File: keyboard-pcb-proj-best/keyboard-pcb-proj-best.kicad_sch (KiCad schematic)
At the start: 0 parts

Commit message: Built Schematic
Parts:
- added C1: 1uF, Capacitor_SMD:C_0805_2012Metric_Pad1.18x1.45mm_HandSolder, symbol Device:C_Small
- added C2, C3, C4: 0.1uF, Capacitor_SMD:C_0805_2012Metric_Pad1.18x1.45mm_HandSolder, symbol Device:C_Small
- added C5: 10uf, Capacitor_SMD:C_0805_2012Metric_Pad1.18x1.45mm_HandSolder, symbol Device:C_Small
- added C6, C7: 22pF, Capacitor_SMD:C_0805_2012Metric_Pad1.18x1.45mm_HandSolder, symbol Device:C_Small
- added D1, D2, D3, D4: SOD-123, Diode_SMD:D_SOD-123, symbol Device:D_Small
- added F1: 500mA, Fuse:Fuse_1206_3216Metric, symbol Device:Polyfuse
- added MX1, MX2, MX3, MX4: MX-NoLED, MX_Alps_Hybrid:MX-10U-NoLED, symbol MX_Alps_Hybrid:MX-NoLED
- added R1, R4: 10k, Resistor_SMD:R_0805_2012Metric, symbol Device:R_Small
- added R2, R3: 22, Resistor_SMD:R_0805_2012Metric, symbol Device:R_Small
- added SW1: SW_PUSH, random-keyboard-parts:SKQG-1155865, symbol keyboard_parts:SW_PUSH
- added U1: ATmega32U4-A, Package_QFP:TQFP-44_10x10mm_P0.8mm, symbol MCU_Microchip_ATmega:ATmega32U4-A
- added USB1: Molex-0548190589, random-keyboard-parts:Molex-0548190589, symbol random-keyboard-parts:Molex-0548190589
- added Y1: 16Mhz, Crystal:Crystal_SMD_3225-4Pin_3.2x2.5mm, symbol Device:Crystal_GND24_Small
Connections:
- new net: R4.2, SW1.2, U1.13 (~{RESET})
- new net: C7.2, U1.16 (XTAL2), Y1.3
- new net: C6.2, U1.17 (XTAL1), Y1.1
- new net: R3.1, U1.3 (D-)
- new net: R1.2, U1.33 (~{HWB}/PE2)
- new net: R2.1, U1.4 (D+)
- new net: C1.1, U1.6 (UCAP)
- new net: D2.2 (A), MX2.2 (ROW)
- new net: D3.2 (A), MX3.2 (ROW)
- new net: D4.2 (A), MX4.2 (ROW)
- new net: D1.2 (A), MX1.2 (ROW)
- new net +5V: C2.1, C3.1, C4.1, C5.1, F1.1, R4.1, U1.14 (VCC), U1.2 (UVCC), U1.24 (AVCC), U1.34 (VCC), U1.44 (AVCC), U1.7 (VBUS)
- new net COL0: MX1.1 (COL), MX3.1 (COL)
- new net COL1: MX2.1 (COL), MX4.1 (COL)
- new net D+: R2.2, USB1.3 (D+)
- new net D-: R3.2, USB1.4 (D-)
- new net GND: C1.2, C2.2, C3.2, C4.2, C5.2, C6.1, C7.1, R1.1, SW1.1, U1.15 (GND), U1.23 (GND), U1.35 (GND), U1.43 (GND), U1.5 (UGND), USB1.1 (GND), Y1.2, Y1.4
- new net ROW0: D1.1 (K), D2.1 (K)
- new net ROW1: D3.1 (K), D4.1 (K)
- new net VCC: F1.2, USB1.5 (VBUS)

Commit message: Created PCB
Still need to finish routing
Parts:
- MX1, MX2, MX3, MX4: footprint MX_Alps_Hybrid:MX-10U-NoLED -> MX_Alps_Hybrid:MX-1U-NoLED
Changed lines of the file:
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@@
 			)
 		)
-		(property "Footprint" "MX_Alps_Hybrid:MX-10U-NoLED"
+		(property "Footprint" "MX_Alps_Hybrid:MX-1U-NoLED"
 			(at 146.685 90.805 0)
 			(effects
@@
 			)
 		)
-		(property "Footprint" "MX_Alps_Hybrid:MX-10U-NoLED"
+		(property "Footprint" "MX_Alps_Hybrid:MX-1U-NoLED"
 			(at 132.715 107.315 0)
 			(effects
@@
 			)
 		)
-		(property "Footprint" "MX_Alps_Hybrid:MX-10U-NoLED"
+		(property "Footprint" "MX_Alps_Hybrid:MX-1U-NoLED"
 			(at 132.715 90.805 0)
 			(effects
@@
 			)
 		)
-		(property "Footprint" "MX_Alps_Hybrid:MX-10U-NoLED"
+		(property "Footprint" "MX_Alps_Hybrid:MX-1U-NoLED"
 			(at 146.685 107.315 0)
 			(effects

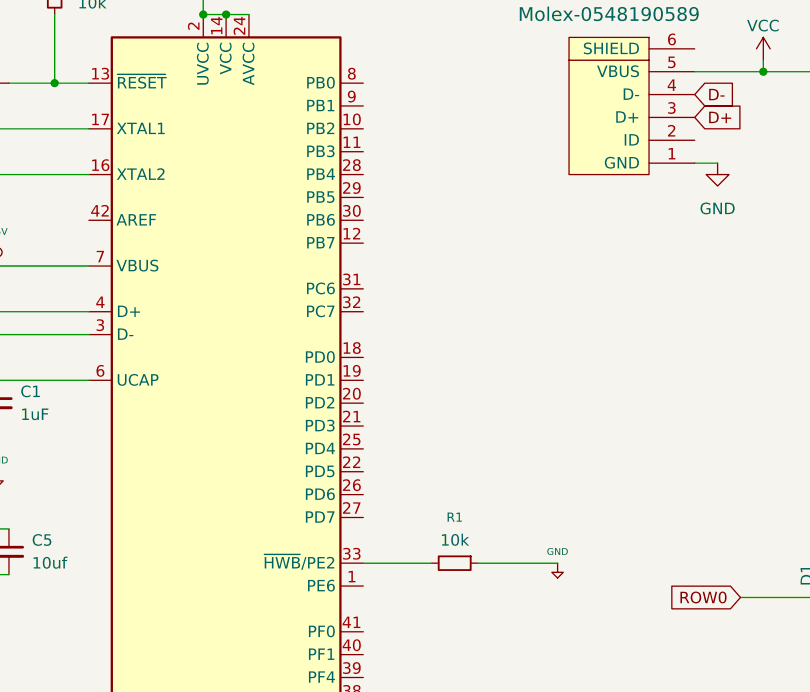
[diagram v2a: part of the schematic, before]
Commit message: Finalized Routing and Matrix Pin Out
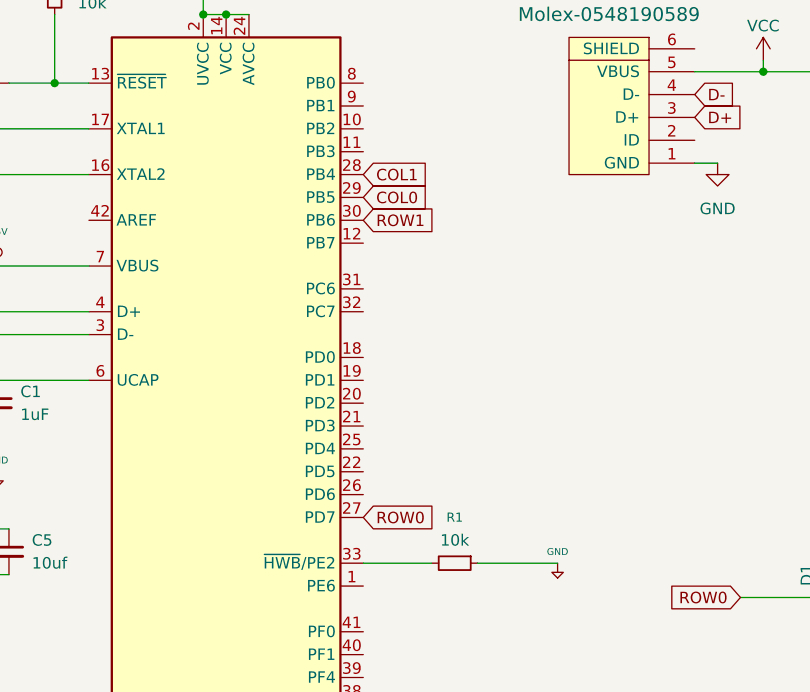
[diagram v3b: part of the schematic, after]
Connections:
- net COL0: now also U1.29 (PB5)
- net COL1: now also U1.28 (PB4)
- net ROW0: now also U1.27 (PD7)
- net ROW1: now also U1.30 (PB6)
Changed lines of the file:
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@@
+		)
+	)
+	(global_label "COL1"
+		(shape input)
+		(at 88.9 53.34 0)
+		(fields_autoplaced yes)
+		(effects
+			(font
+				(size 1.27 1.27)
+			)
+			(justify left)
+		)
+		(property "Intersheetrefs" "${INTERSHEET_REFS}"
+			(at 96.7233 53.34 0)
+			(effects
+				(font
+					(size 1.27 1.27)
+				)
+				(justify left)
+				(hide yes)
+			)
 		)
 	)
@@
 		)
 	)
+	(global_label "ROW1"
+		(shape input)
+		(at 88.9 58.42 0)
+		(fields_autoplaced yes)
+		(effects
+			(font
+				(size 1.27 1.27)
+			)
+			(justify left)
+		)
+		(property "Intersheetrefs" "${INTERSHEET_REFS}"
+			(at 97.1466 58.42 0)
+			(effects
+				(font
+					(size 1.27 1.27)
+				)
+				(justify left)
+				(hide yes)
+			)
+		)
+	)
 	(global_label "D-"
 		(shape input)
@@
 		)
 	)
+	(global_label "ROW0"
+		(shape input)
+		(at 88.9 91.44 0)
+		(fields_autoplaced yes)
+		(effects
+			(font
+				(size 1.27 1.27)
+			)
+			(justify left)
+		)
+		(property "Intersheetrefs" "${INTERSHEET_REFS}"
+			(at 97.1466 91.44 0)
+			(effects
+				(font
+					(size 1.27 1.27)
+				)
+				(justify left)
+				(hide yes)
+			)
+		)
+	)
 	(global_label "D+"
 		(shape input)
@@
 				(hide yes)
 			)
+		)
+	)
+	(global_label "COL0"
+		(shape input)
+		(at 88.9 55.88 0)
+		(fields_autoplaced yes)
+		(effects
+			(font
+				(size 1.27 1.27)
+			)
+			(justify left)
+		)
+		(property "Intersheetrefs" "${INTERSHEET_REFS}"
+			(at 96.7233 55.88 0)
+			(effects
+				(font
+					(size 1.27 1.27)
+				)
+				(justify left)
+				(hide yes)
+			)
